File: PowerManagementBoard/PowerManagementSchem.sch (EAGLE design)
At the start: 112 parts, among them J1 D15S24A4GV00LF, J8 182-037-213R531, J9 182-025-213R531, Q1 PMOSFET, Q10 PMOSFET, Q11 PMOSFET, Q12 PMOSFET, Q2 PMOSFET, Q3 PMOSFET, Q4 PMOSFET, Q5 PMOSFET, Q6 PMOSFET, Q7 PMOSFET, Q8 PMOSFET, Q9 PMOSFET, U1 VX7805-500, U2 PYB20-Q24-S5, U3 PYB30-Q48-S5, U4 PYB30-Q48-S12, U5 3V3REG, U6 INA4180-SPLIT, U7 INA4180-SPLIT, U8 TEENSY-4.0SILK, U9 INA4180-SPLIT

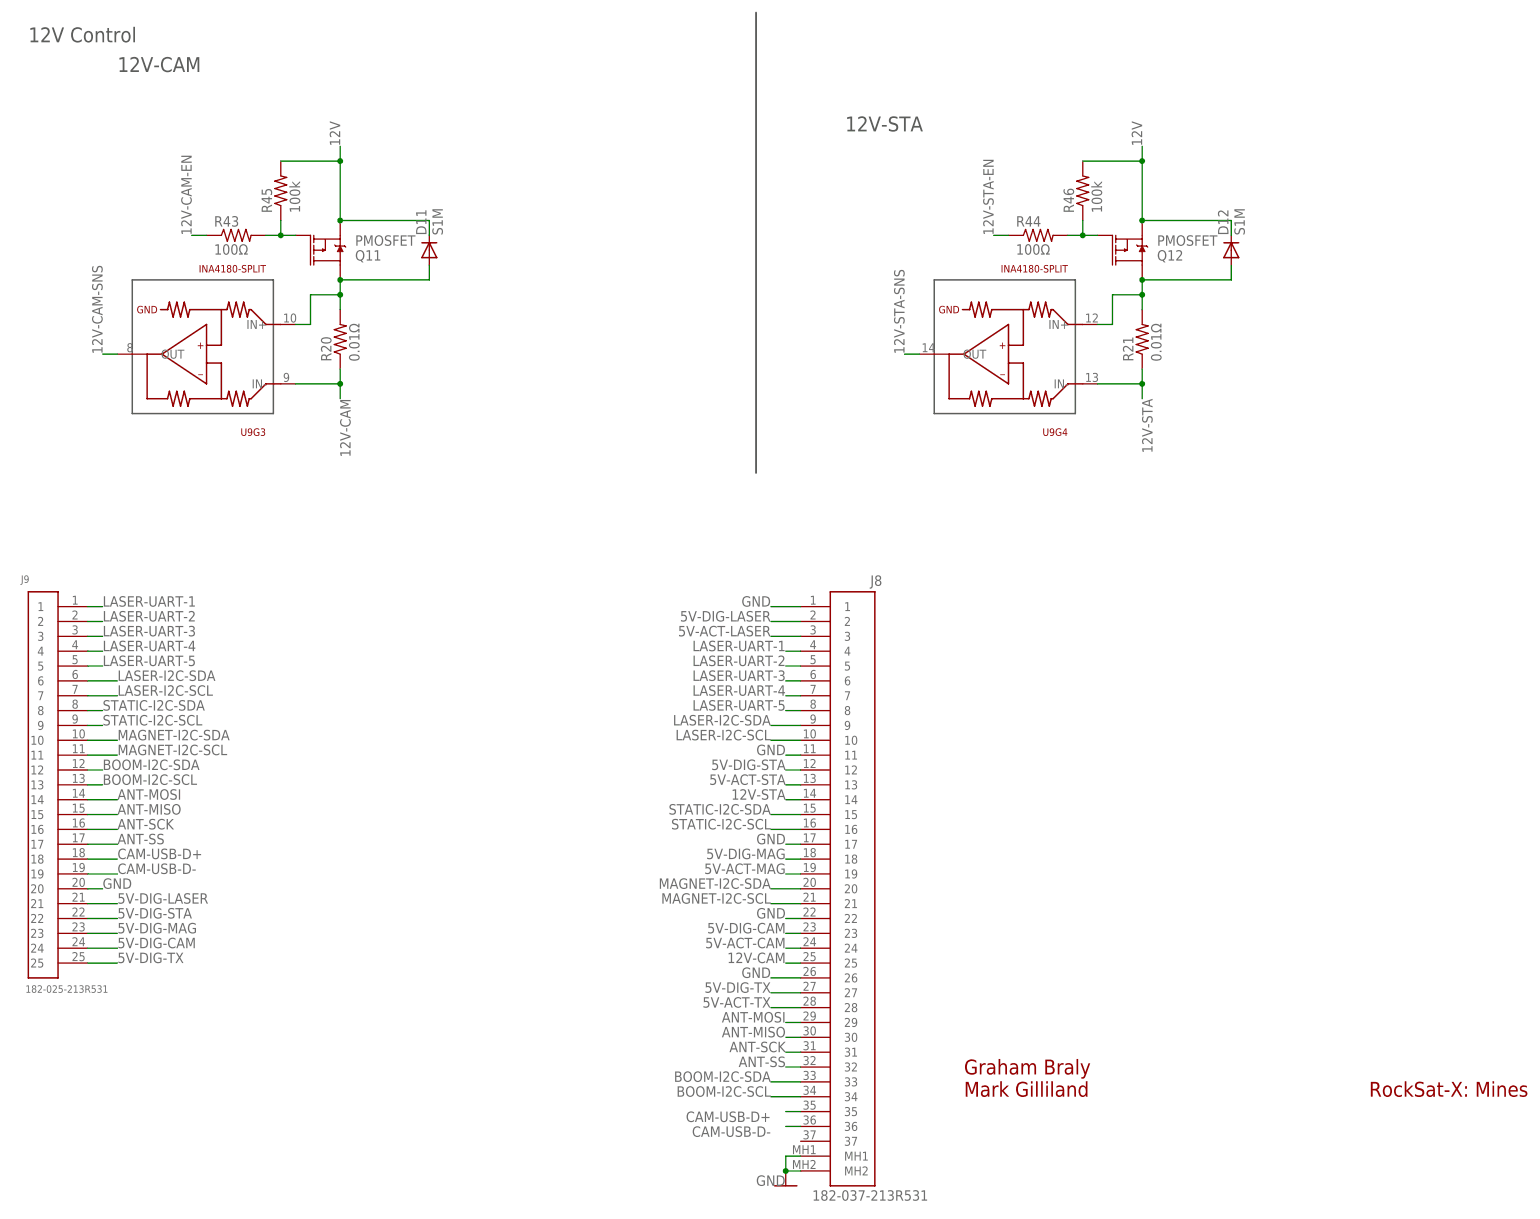
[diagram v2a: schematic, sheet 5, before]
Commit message: Gateswapped the op-amps around so that we get easier routing
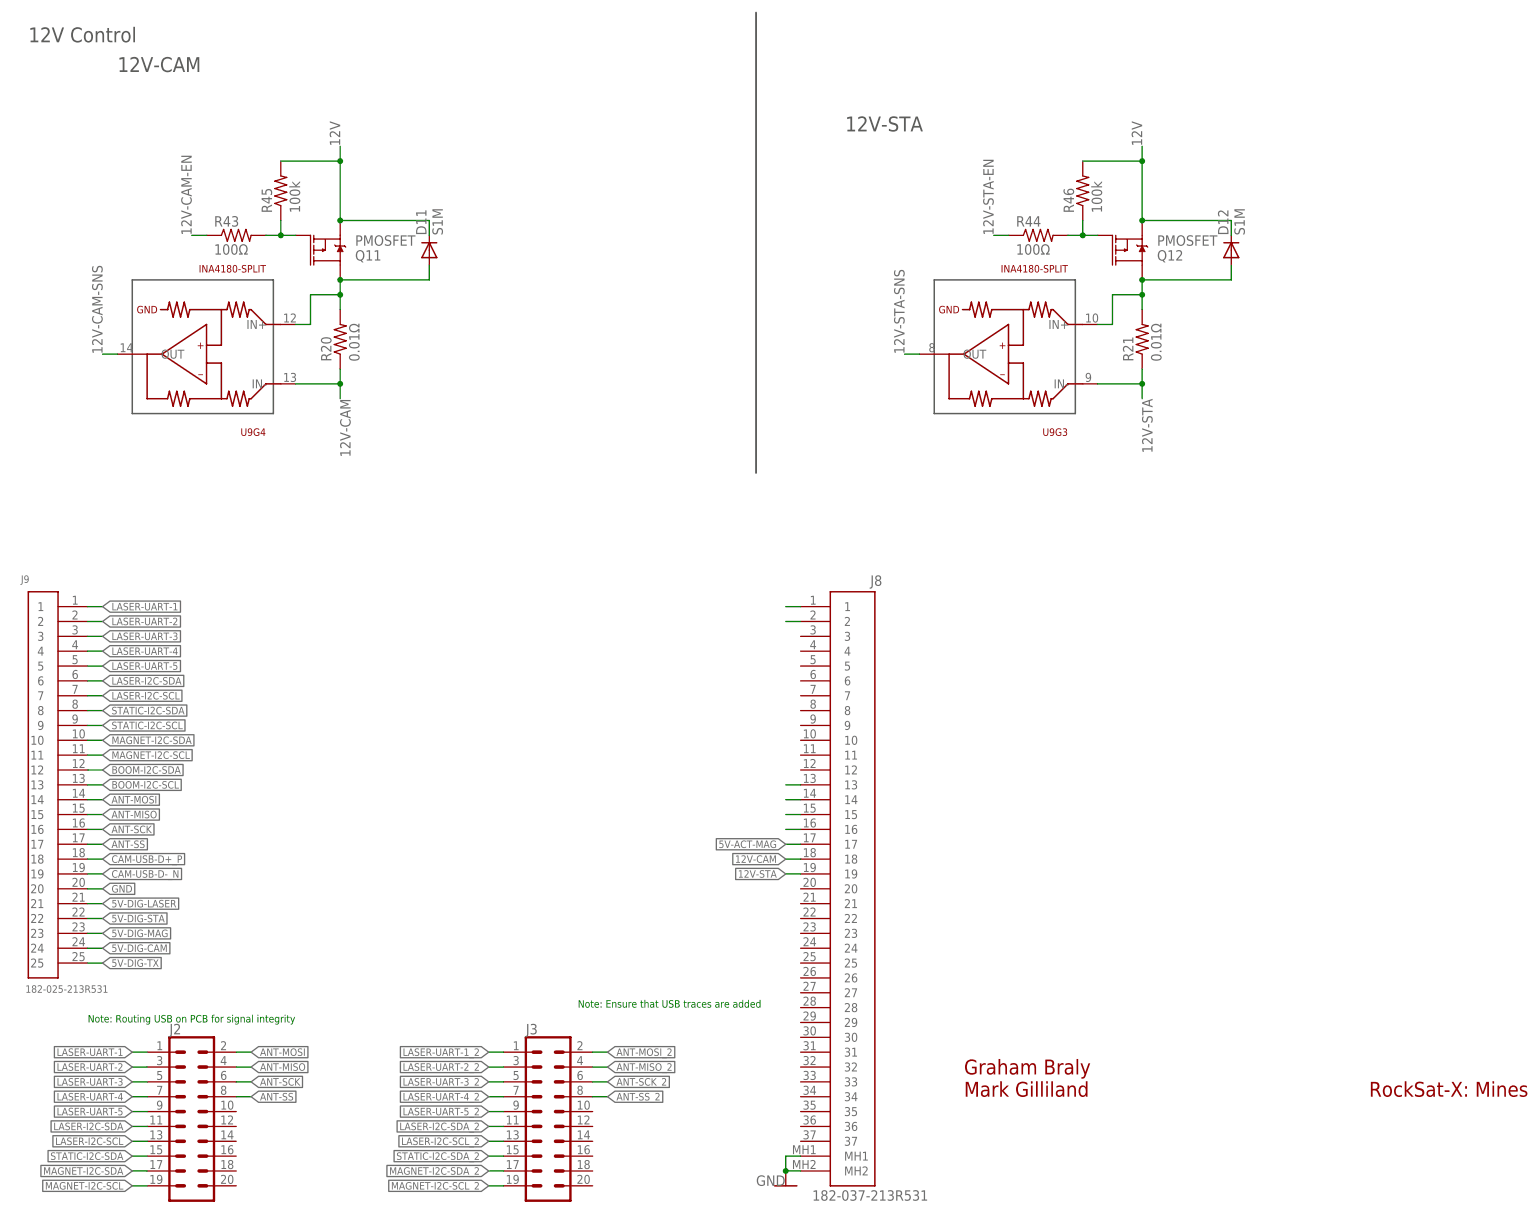
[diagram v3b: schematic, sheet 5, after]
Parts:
- added J2, J3: (no value), SparkFun-Connectors:CONN_10X22X10_LOCK
- added TP2, TP3, TP4, TP5, TP6, TP7, TP8, TP9: TPPAD1-13, testpad:TPPAD1-13
- TP_12V_CTRL, TP_5V-ACT_CTRL, TP_5V-DIG_CTRL: value TPTP15R -> TPPAD1-13; device testpad:TPTP15R -> testpad:TPPAD1-13
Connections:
- net N$1 renamed 12V-CTRL
- net N$2 renamed 5V-ACT-CTRL
- net N$3 renamed 12V-TRIM
- net N$4 renamed 5V-ACT-TRIM
- net N$6 renamed 5V-DIG-CTRL
- net N$7 renamed 5V-DIG-TRIM
- removed net CAM-USB-D+: J8.35, J9.18
- removed net CAM-USB-D-: J8.36, J9.19
- new net ANT-MISO_2: J3.4
- new net ANT-MOSI_2: J3.2
- new net ANT-SCK_2: J3.6
- new net ANT-SS_2: J3.8
- new net CAM-USB-D+_P: J9.18
- new net CAM-USB-D-_N: J9.19
- new net LASER-I2C-SCL_2: J3.13
- new net LASER-I2C-SDA_2: J3.11
- new net LASER-UART-1_2: J3.1
- new net LASER-UART-2_2: J3.3
- new net LASER-UART-3_2: J3.5
- new net LASER-UART-4_2: J3.7
- new net LASER-UART-5_2: J3.9
- new net MAGNET-I2C-SCL_2: J3.19
- new net MAGNET-I2C-SDA_2: J3.17
- new net N$1: J8.1
- new net N$2: J8.2
- new net N$33: J8.14
- new net N$35: J8.13
- new net N$6: J8.16
- new net N$7: J8.15
- new net STATIC-I2C-SDA_2: J3.15
- net 12V: now also TP9.TP
- net 12V-CAM: now also J8.18, U9G4.IN-; no longer J8.25, U9G3.IN-
- net 12V-CAM-SNS: now also U9G4.OUT; no longer U9G3.OUT
- net 12V-STA: now also J8.19, U9G3.IN-; no longer J8.14, U9G4.IN-
- net 12V-STA-SNS: now also U9G3.OUT; no longer U9G4.OUT
- net 5V-ACT: now also D9.C, Q9.S, TP8.TP; no longer D8.C, Q8.S
- net 5V-ACT-CAM: now also U7G1.IN-; no longer J8.24, U7G2.IN-
- net 5V-ACT-CAM-SNS: now also U7G1.OUT; no longer U7G2.OUT
- net 5V-ACT-LASER: now also U7G4.IN-; no longer J8.3, U6G4.IN-
- net 5V-ACT-LASER-SNS: now also U7G4.OUT; no longer U6G4.OUT
- net 5V-ACT-MAG: now also J8.17, U9G1.IN-; no longer J8.19, U9G2.IN-
- net 5V-ACT-MAG-SNS: now also U9G1.OUT; no longer U9G2.OUT
- net 5V-ACT-STA: now also U9G2.IN-; no longer J8.13, U7G4.IN-
- net 5V-ACT-STA-SNS: now also U9G2.OUT; no longer U7G4.OUT
- net 5V-ACT-TX: now also U7G3.IN-; no longer J8.28, U6G2.IN-
- net 5V-ACT-TX-SNS: now also U7G3.OUT; no longer U6G2.OUT
- net 5V-DIG: now also D8.C, Q8.S, TP7.TP; no longer D9.C, Q9.S
- net 5V-DIG-CAM: now also U6G1.IN-; no longer J8.23, U7G1.IN-
- net 5V-DIG-CAM-SNS: now also U6G1.OUT; no longer U7G1.OUT
- net 5V-DIG-LASER: now also U6G4.IN-; no longer J8.2, U6G3.IN-
- net 5V-DIG-LASER-SNS: now also U6G4.OUT; no longer U6G3.OUT
- net 5V-DIG-MAG: now also U6G3.IN-; no longer J8.18, U9G1.IN-
- net 5V-DIG-MAG-SNS: now also U6G3.OUT; no longer U9G1.OUT
- net 5V-DIG-STA: now also U7G2.IN-; no longer J8.12, U7G3.IN-
- net 5V-DIG-STA-SNS: now also U7G2.OUT; no longer U7G3.OUT
- net 5V-DIG-TX: now also U6G2.IN-; no longer J8.27, U6G1.IN-
- net 5V-DIG-TX-SNS: now also U6G2.OUT; no longer U6G1.OUT
- net ANT-MISO: now also J2.4; no longer J8.30
- net ANT-MOSI: now also J2.2; no longer J8.29
- net ANT-SCK: now also J2.6; no longer J8.31
- net ANT-SS: now also J2.8; no longer J8.32
- net BOOM-I2C-SCL: no longer J8.34
- net BOOM-I2C-SDA: no longer J8.33
- net GND: no longer J8.1, J8.11, J8.17, J8.22, J8.26, U7G$5.GND, U9G$5.GND
- net LASER-I2C-SCL: now also J2.13; no longer J8.10
- net LASER-I2C-SDA: now also J2.11; no longer J8.9
- net LASER-UART-1: now also J2.1; no longer J8.4
- net LASER-UART-2: now also J2.3; no longer J8.5
- net LASER-UART-3: now also J2.5; no longer J8.6
- net LASER-UART-4: now also J2.7; no longer J8.7
- net LASER-UART-5: now also J2.9; no longer J8.8
- net MAGNET-I2C-SCL: now also J2.19; no longer J8.21
- net MAGNET-I2C-SDA: now also J2.17; no longer J8.20
- net MNGR-3.3V: now also TP6.TP; no longer U7G$5.V+, U9G$5.V+
- net MNGR-5V: now also TP5.TP
- net N$11: now also U6G2.IN+; no longer U6G1.IN+
- net N$12: now also U7G3.IN+; no longer U6G2.IN+
- net N$14: now also U6G4.IN+; no longer U6G3.IN+
- net N$16: now also U7G4.IN+; no longer U6G4.IN+
- net N$22: now also U9G1.IN+; no longer U9G2.IN+
- net N$23: now also Q8.G; no longer Q9.G
- net N$24: now also D8.A, Q8.D, U6G3.IN+; no longer D9.A, Q9.D, U9G1.IN+
- net N$25: now also Q9.G; no longer Q8.G
- net N$26: now also D9.A, Q9.D, U9G2.IN+; no longer D8.A, Q8.D, U7G4.IN+
- net N$28: now also U7G2.IN+; no longer U7G3.IN+
- net N$30: now also U7G1.IN+; no longer U7G2.IN+
- net N$32: now also U6G1.IN+; no longer U7G1.IN+
- net N$34: now also U9G4.IN+; no longer U9G3.IN+
- net N$36: now also U9G3.IN+; no longer U9G4.IN+
- net STATIC-I2C-SCL: no longer J8.16
- net STATIC-I2C-SDA: now also J2.15; no longer J8.15
- net SUPPLY_FOR_5V-DIG: now also TP2.TP
- net SUPPLY_FOR_ACT: now also TP3.TP
- net SUPPLY_FOR_MNGR: now also TP4.TP
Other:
- note added: "Note: Ensure that USB traces are added"
- note added: "Note: Routing USB on PCB for signal integrity"
- moved on the sheet: D8, D9, Q8, Q9, U6G2, U6G4, U7G1, U7G2, U9G1, U9G2, U9G3, U9G4

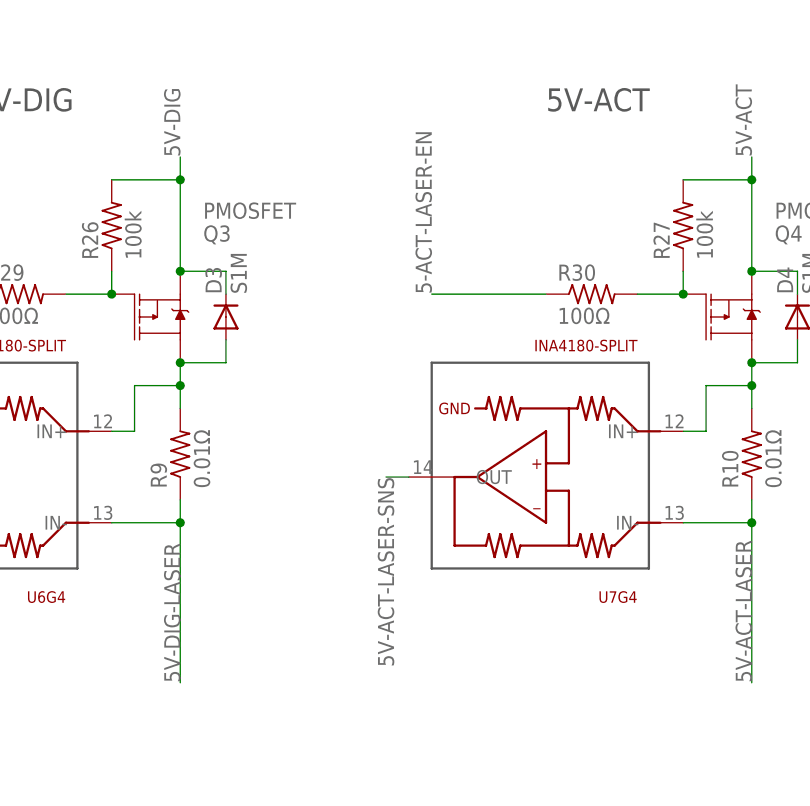
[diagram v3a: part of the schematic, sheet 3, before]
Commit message: CurrentAmps routed
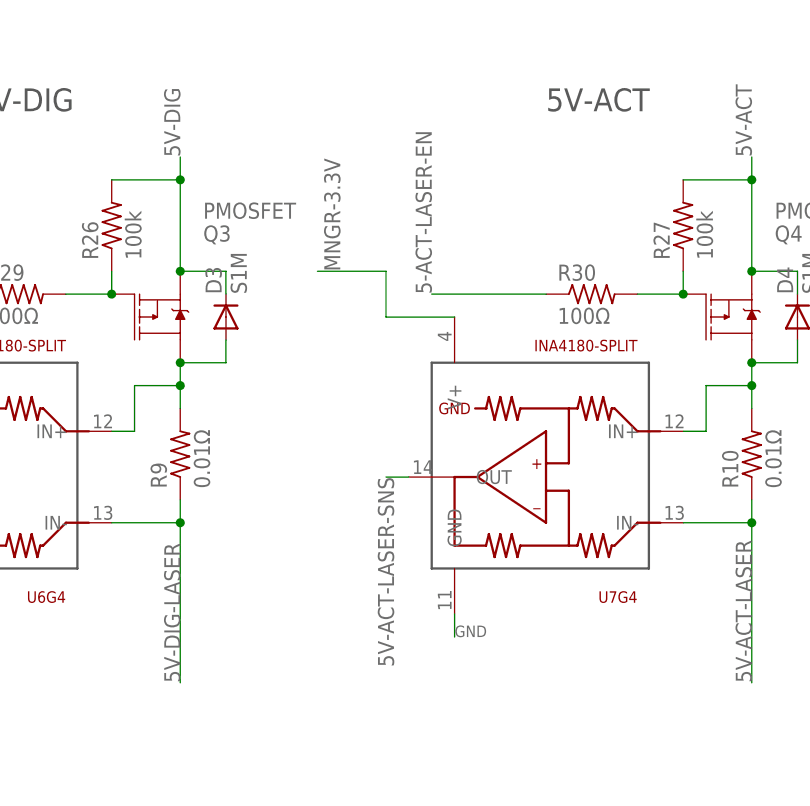
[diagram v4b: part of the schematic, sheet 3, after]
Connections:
- net GND: now also U7G$5.GND, U9G$5.GND
- net MNGR-3.3V: now also U7G$5.V+, U9G$5.V+
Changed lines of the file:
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@@
 <attribute name="VALUE" x="116.84" y="172.72" size="1.27" layer="94" rot="R180"/>
 </instance>
+<instance part="U7" gate="G$5" x="231.14" y="172.72" smashed="yes"/>
 </instances>
 <busses>
@@
 <pinref part="GND17" gate="1" pin="GND"/>
 </segment>
+<segment>
+<pinref part="U7" gate="G$5" pin="GND"/>
+<wire x1="231.14" y1="144.78" x2="231.14" y2="142.24" width="0.1524" layer="91"/>
+<label x="231.14" y="142.24" size="1.27" layer="95"/>
+</segment>
 </net>
 <net name="MNGR-3.3V" class="0">
@@
 <wire x1="30.48" y1="175.26" x2="30.48" y2="190.5" width="0.1524" layer="91"/>
 <label x="30.48" y="177.8" size="1.778" layer="95" rot="R90"/>
+</segment>
+<segment>
+<pinref part="U7" gate="G$5" pin="V+"/>
+<wire x1="231.14" y1="177.8" x2="223.52" y2="177.8" width="0.1524" layer="91"/>
+<wire x1="223.52" y1="177.8" x2="223.52" y2="182.88" width="0.1524" layer="91"/>
+<wire x1="223.52" y1="182.88" x2="215.9" y2="182.88" width="0.1524" layer="91"/>
+<label x="218.44" y="182.88" size="1.778" layer="95" rot="R90"/>
 </segment>
 </net>
@@
 <attribute name="VALUE" x="116.84" y="71.12" size="1.27" layer="94" rot="R180"/>
 </instance>
+<instance part="U9" gate="G$5" x="96.52" y="68.58" smashed="yes" rot="MR0"/>
 </instances>
 <busses>
@@
 </segment>
 </net>
+<net name="MNGR-3.3V" class="0">
+<segment>
+<pinref part="U9" gate="G$5" pin="V+"/>
+<wire x1="96.52" y1="73.66" x2="91.44" y2="73.66" width="0.1524" layer="91"/>
+<wire x1="91.44" y1="73.66" x2="91.44" y2="76.2" width="0.1524" layer="91"/>
+<label x="91.44" y="76.2" size="1.778" layer="95" rot="R90"/>
+</segment>
+</net>
+<net name="GND" class="0">
+<segment>
+<pinref part="U9" gate="G$5" pin="GND"/>
+<wire x1="96.52" y1="40.64" x2="96.52" y2="35.56" width="0.1524" layer="91"/>
+<label x="96.52" y="35.56" size="1.778" layer="95"/>
+</segment>
+</net>

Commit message: More routing
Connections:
- removed net 5-ACT-LASER-EN: R30.1
- removed net N$33: J8.14
- removed net N$6: J8.16
- removed net N$7: J8.15
- net 12V-CAM-SNS: now also U$18.CH0; no longer U$18.CH5
- net 12V-STA-SNS: now also U$18.CH3; no longer U$19.CH5
- net 5V-ACT-CAM-SNS: now also U$19.CH3; no longer U$19.CH2
- net 5V-ACT-LASER: now also J8.14
- net 5V-ACT-LASER-EN: now also R30.1
- net 5V-ACT-LASER-SNS: now also U$18.CH4; no longer U$19.CH1
- net 5V-ACT-MAG-SNS: now also U$18.CH1; no longer U$19.CH3
- net 5V-ACT-STA: now also J8.16
- net 5V-ACT-STA-SNS: now also U$18.CH6; no longer U$19.CH4
- net 5V-ACT-TX: now also J8.15
- net 5V-ACT-TX-SNS: now also U$18.CH2; no longer U$19.CH0
- net 5V-DIG-CAM-SNS: now also U$19.CH2; no longer U$18.CH2
- net 5V-DIG-LASER-SNS: now also U$19.CH6; no longer U$18.CH1
- net 5V-DIG-MAG-SNS: now also U$19.CH1; no longer U$18.CH3
- net 5V-DIG-STA-SNS: now also U$19.CH0; no longer U$18.CH4
- net 5V-DIG-TX-SNS: now also U$19.CH4; no longer U$18.CH0
- net BOOM-I2C-SCL: now also J2.20
- net BOOM-I2C-SDA: now also J2.18
- net LASER-I2C-SCL: now also J2.11; no longer J2.13
- net LASER-I2C-SDA: now also J2.10; no longer J2.11
- net MAGNET-I2C-SCL: now also J2.16; no longer J2.19
- net MAGNET-I2C-SDA: now also J2.13; no longer J2.17
- net MUX-SEL-A: now also U8.A7/21*; no longer U8.A3/17
- net MUX-SEL-C: now also U8.A5/19/SCL0; no longer U8.A7/21*
- net STATIC-I2C-SCL: now also J2.14
- net STATIC-I2C-SDA: now also J2.12; no longer J2.15
